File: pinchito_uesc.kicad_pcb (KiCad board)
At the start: 2 copper layers, 21.7 x 14.1 mm, 21 parts, among them J1 Conn_01x03_Pin, J2 Conn_01x03_Pin, Q1 AO6604_C709896, Q2 AO6604_C709896, Q3 AO6604_C709896, Q4 AO6604_C5182068, Q5 AO6604_C5182068, Q6 AO6604_C5182068, U1 EFM8BB21F16G-C-QFN20

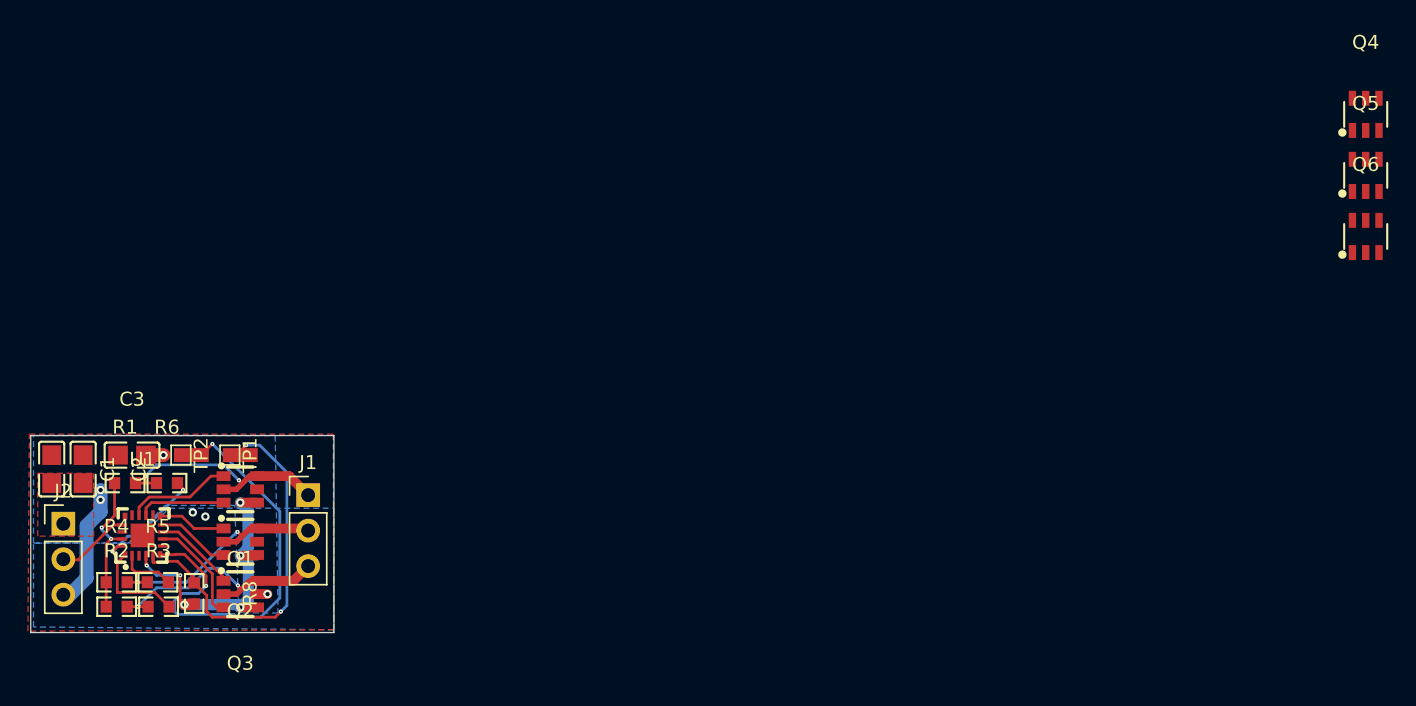
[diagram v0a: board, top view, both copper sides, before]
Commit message: Bump design to new MOSFETs
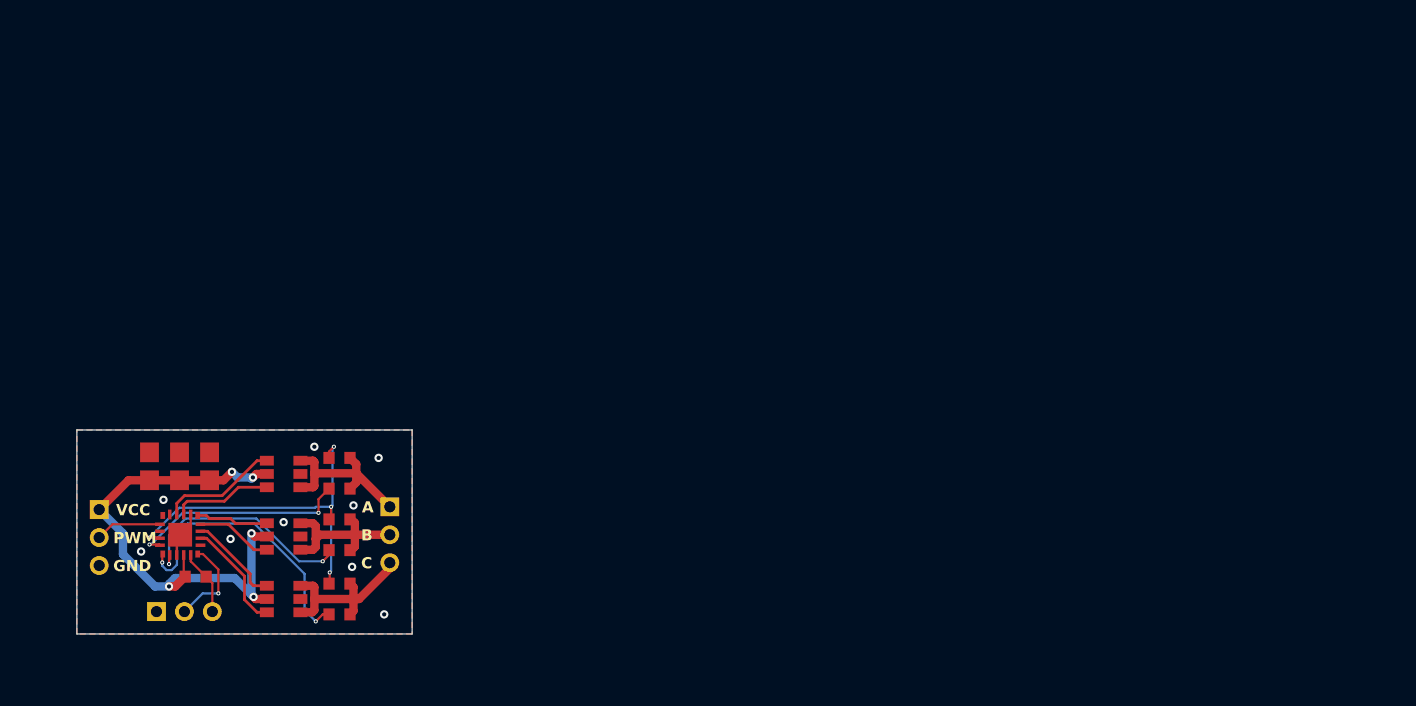
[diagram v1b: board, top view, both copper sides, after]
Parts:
- removed Q4, Q5, Q6: AO6604_C5182068, component_lib:SOT-23-6_L2.9-W1.6-P0.95-LS2.8-BL
- removed TP1, TP2: TestPoint, TestPoint:TestPoint_Pad_1.0x1.0mm
- added J3: Prog, Connector_PinHeader_2.00mm:PinHeader_1x03_P2.00mm_Vertical, F.Cu at (167.0, 71.2)
- J1: value Conn_01x03_Pin -> Motor; footprint Connector_PinHeader_2.54mm:PinHeader_1x03_P2.54mm_Vertical -> Connector_PinHeader_2.00mm:PinHeader_1x03_P2.00mm_Vertical
- J2: value Conn_01x03_Pin -> Power; footprint Connector_PinHeader_2.54mm:PinHeader_1x03_P2.54mm_Vertical -> Connector_PinHeader_2.00mm:PinHeader_1x03_P2.00mm_Vertical
- Q1, Q2, Q3: value AO6604_C709896 -> AO6604
- moved R4 16.6 mm to (180.1, 64.6)
- moved R2 16.0 mm to (180.1, 69.2)
- moved R1 15.5 mm to (180.1, 60.2)
- moved R5 13.2 mm to (180.1, 66.8), turned to 180 degrees
- moved R3 13.0 mm to (180.1, 71.4), turned to 180 degrees
- moved R6 12.4 mm to (180.1, 62.4), turned to 180 degrees
- moved C1 9.15 mm to (168.7, 60.8)
- moved Q3 9.14 mm to (176.1, 61.4)
- moved J1 5.90 mm to (183.7, 63.7)
- moved C3 5.61 mm to (170.8, 60.8), turned to -90 degrees
- moved Q2 5.14 mm to (176.1, 70.3)
- moved C2 4.75 mm to (166.5, 60.8)
- moved Q1 4.58 mm to (176.1, 65.8)
- moved J2 2.76 mm to (162.9, 63.9)
- moved U1 2.70 mm to (168.7, 65.7)
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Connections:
- Q1 pad 2: /M_A -> /VCC
- Q1 pad 4: /VCC -> /M_B
- Q1 pad 6: /M_A -> /M_B
- Q2 pad 2: /M_B -> /VCC
- Q2 pad 4: /VCC -> /M_C
- Q2 pad 6: /M_B -> /M_C
- Q3 pad 2: /M_C -> /VCC
- Q3 pad 4: /VCC -> /M_A
- Q3 pad 6: /M_C -> /M_A
- U1 pad 10: Net-(Q2-G2) -> Net-(Q1-G2)
- U1 pad 11: Net-(Q2-G1) -> Net-(Q1-G1)
- U1 pad 13: Net-(Q1-G2) -> Net-(Q3-G2)
- U1 pad 14: Net-(Q1-G1) -> Net-(Q3-G1)
- U1 pad 8: Net-(Q3-G2) -> Net-(Q2-G2)
- U1 pad 9: Net-(Q3-G1) -> Net-(Q2-G1)
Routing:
- net /C2D: track 31.3 -> 6.62 mm, vias 2 -> 1
- net /C2CK: track 27.1 -> 4.69 mm, vias 2 -> 0
- net /FCom: track 10.5 -> 26.5 mm, vias 2 -> 4
- net /VCC: track 23.7 -> 38.3 mm, vias 7 -> 5
- net Net-(U1-P0.1): track 7.06 -> 20.2 mm, vias 0 -> 2
- net Net-(U1-P0.0): track 3.94 -> 16.5 mm, vias 0 -> 2
- net Net-(U1-P0.2): track 8.40 -> 15.9 mm
- net GND: track 9.70 -> 3.31 mm, vias 5 -> 9
- net /M_C: track 19.1 -> 12.9 mm, vias 2 -> 0
- net /M_B: track 17.1 -> 11.7 mm, vias 2 -> 0
- net /M_A: track 16.7 -> 12.7 mm, vias 2 -> 0
- net Net-(Q2-G2): track 5.24 -> 7.93 mm
- net Net-(Q3-G1): track 5.96 -> 8.51 mm
- net Net-(Q1-G1): track 7.55 -> 5.20 mm
- net Net-(Q2-G1): track 4.91 -> 6.72 mm
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- removed copper zone on B.Cu, net /VCC
- removed copper zone on F.Cu, net /VCC
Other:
- board size 21.7 x 14.1 mm -> 24 x 14.6 mm
- board text added: "A"
- board text added: "B"
- board text added: "C"
- board text added: "CLK"
- board text added: "DATA"
- board text added: "GND"
- board text added: "PROG"
- board text added: "PWM"
- board text added: "Pinchito Edition"
- board text added: "VCC"
- board text added: "μESC"

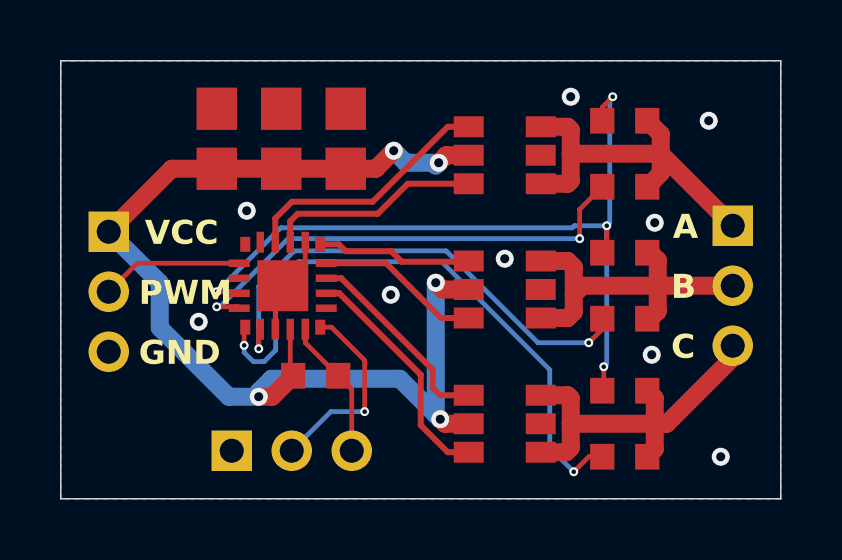
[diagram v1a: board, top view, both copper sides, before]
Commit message: Round Corners
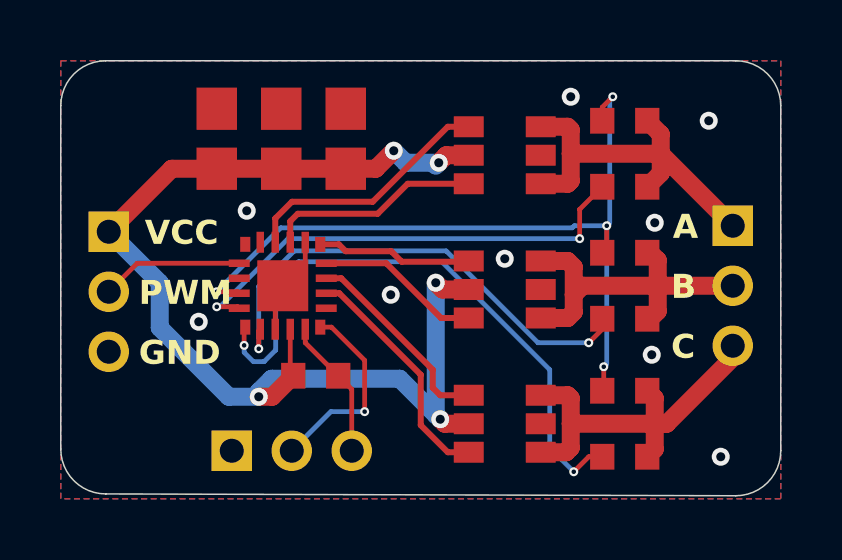
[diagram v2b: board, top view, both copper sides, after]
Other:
- board size 24 x 14.6 mm -> 24 x 14.5 mm
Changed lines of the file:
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@@
 	(generator_version "8.0")
 	(general
-		(thickness 1.6)
+		(thickness 1.09)
 		(legacy_teardrops no)
 	)
@@
 	)
 	(setup
+		(stackup
+			(layer "F.SilkS"
+				(type "Top Silk Screen")
+			)
+			(layer "F.Paste"
+				(type "Top Solder Paste")
+			)
+			(layer "F.Mask"
+				(type "Top Solder Mask")
+				(thickness 0.01)
+			)
+			(layer "F.Cu"
+				(type "copper")
+				(thickness 0.035)
+			)
+			(layer "dielectric 1"
+				(type "core")
+				(thickness 1)
+				(material "FR4")
+				(epsilon_r 4.5)
+				(loss_tangent 0.02)
+			)
+			(layer "B.Cu"
+				(type "copper")
+				(thickness 0.035)
+			)
+			(layer "B.Mask"
+				(type "Bottom Solder Mask")
+				(thickness 0.01)
+			)
+			(layer "B.Paste"
+				(type "Bottom Solder Paste")
+			)
+			(layer "B.SilkS"
+				(type "Bottom Silk Screen")
+			)
+			(copper_finish "None")
+			(dielectric_constraints no)
+		)
 		(pad_to_mask_clearance 0)
 		(allow_soldermask_bridges_in_footprints no)
@@
 		(layer "B.SilkS")
 	)
-	(gr_rect
-		(start 161.3 58.2)
-		(end 185.3 72.8)
+	(gr_line
+		(start 185.3 59.7)
+		(end 185.3 71.2)
+		(stroke
+			(width 0.05)
+			(type default)
+		)
+		(layer "Edge.Cuts")
+	)
+	(gr_line
+		(start 183.8 72.7)
+		(end 162.8 72.63934)
+		(stroke
+			(width 0.05)
+			(type default)
+		)
+		(layer "Edge.Cuts")
+	)
+	(gr_line
+		(start 162.8 58.2)
+		(end 183.8 58.2)
+		(stroke
+			(width 0.05)
+			(type default)
+		)
+		(layer "Edge.Cuts")
+	)
+	(gr_arc
+		(start 185.3 71.2)
+		(mid 184.86066 72.26066)
+		(end 183.8 72.7)
+		(stroke
+			(width 0.05)
+			(type default)
+		)
+		(layer "Edge.Cuts")
+	)
+	(gr_arc
+		(start 183.8 58.2)
+		(mid 184.86066 58.63934)
+		(end 185.3 59.7)
+		(stroke
+			(width 0.05)
+			(type default)
+		)
+		(layer "Edge.Cuts")
+	)
+	(gr_line
+		(start 161.3 59.7)
+		(end 161.3 71.13934)
+		(stroke
+			(width 0.05)
+			(type default)
+		)
+		(layer "Edge.Cuts")
+	)
+	(gr_arc
+		(start 162.8 72.63934)
+		(mid 161.73934 72.2)
+		(end 161.3 71.13934)
+		(stroke
+			(width 0.05)
+			(type default)
+		)
+		(layer "Edge.Cuts")
+	)
+	(gr_arc
+		(start 161.3 59.7)
+		(mid 161.73934 58.63934)
+		(end 162.8 58.2)
 		(stroke
 			(width 0.05)
 			(type default)
 		)
-		(fill none)
 		(layer "Edge.Cuts")
 	)
